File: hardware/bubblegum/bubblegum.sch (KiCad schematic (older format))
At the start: 107 parts, among them P1 RX_OUT, P2 RX_ONLY, P3 SERIAL, P4 TX/RX, P5 CONN_2, P6 TX_IN, P7 VCC, P8 SWITCH_CTRL, Q1 MOSFET_P, Q2 MOSFET_N, Q3 MOSFET_P, Q4 MOSFET_N, T1 RX_IF_BALUN, T2 RX_BALUN, T4 TX_BALUN, T6 TX_IF_BALUN, U10 TX_HIGHPASS_FILTER, U11 PE4140, U12 SKY13350, U13 TX_LOWPASS_FILTER, U16 GSG-74HC04, U3 RX_HIGHPASS_FILTER, U4 SKY13350, U5 SKY13350, U6 PE4140, U7 RX_LOWPASS_FILTER, U8 SKY13350, U9 TRF3765

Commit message: loop filter values for PFD at 1.6 MHz
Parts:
- C31: value C -> 47pF
- C32: value C -> 560pF
- C33: value C -> 4p7
- C34: value C -> DNP
- R13: value R -> 10k
- R6: value R -> 5k
- R7: value R -> 0
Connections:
- wire segments 354 -> 355
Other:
- note added: "loop filter\n(1.6 MHz)"
- note removed: "loop filter"

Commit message: noticed bias problem with LO bypass mode
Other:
- note added: "FIXME: This should be pulled below GND in bypass\nmode, or perhaps everything could be biased to 1V8\nin normal mode."
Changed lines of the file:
@@
-EESchema Schematic File Version 2  date Sat Jun 30 12:21:44 2012
+EESchema Schematic File Version 2  date Sun Jul  1 07:30:52 2012
 LIBS:power
 LIBS:device
@@
 Sheet 1 1
 Title ""
-Date "30 jun 2012"
+Date "1 jul 2012"
 Rev ""
 Comp ""
@@
 Comment4 ""
 $EndDescr
+Text Notes 11100 2450 0    40   ~ 0
+FIXME: This should be pulled below GND in bypass\nmode, or perhaps everything could be biased to 1V8\nin normal mode.
 Connection ~ 13600 6050
 Wire Wire Line

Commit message: fixed LO bypass mode by introducing intermediate mixer bias voltage
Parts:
- removed Q1, Q3: MOSFET_P, symbol MOSFET_P
- removed Q2, Q4, Q? (x2): MOSFET_N, symbol MOSFET_N
- removed R1, R8: 10k, symbol R
- added C? (x2): 1uF, symbol C
- added C? (x8): 100nF, symbol C
- added U? (x2): DMC2400, symbol DMC2400
- added U? (x2): DMN2400, symbol DMC2400
- added U?: NCP699, symbol NCP699
- L3, L4, L5, L6: value INDUCTOR -> 4n7
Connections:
- net labels added: MIX_BIAS, RX_BYPASS, TX_BYPASS
- wire segments 355 -> 406
- no-connect marks 11 -> 9
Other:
- note added: "Bypass control signals allow the LO to be\nbypassed (essentially a zero Hz LO). The LO\nshould be switched off when bypass is enabled."
- note added: "DC connection to MIX_BIAS\nrequired on IF1, IF2?"
- note added: "DC connection to MIX_BIAS\nrequired on RF1, RF2?"
- note added: "balun here may not be needed if\ndirect connection to MAX2837 is made"
- note removed: "Bypass control signals (active low) allow the LO to\nbe bypassed (essentially a zero Hz LO). The LO\nshould be switched off when bypass is enabled."
- note removed: "DC connection to GND required on IF1, IF2?"
- note removed: "DC connection to GND required on RF1, RF2?"
- note removed: "FIXME: This should be pulled below GND in bypass\nmode, or perhaps everything could be biased to 1V8\nin normal mode."
- note removed: "balun here may not not be needed if\ndirect connection to MAX2837 is made"
- moved on the sheet: C?, L6

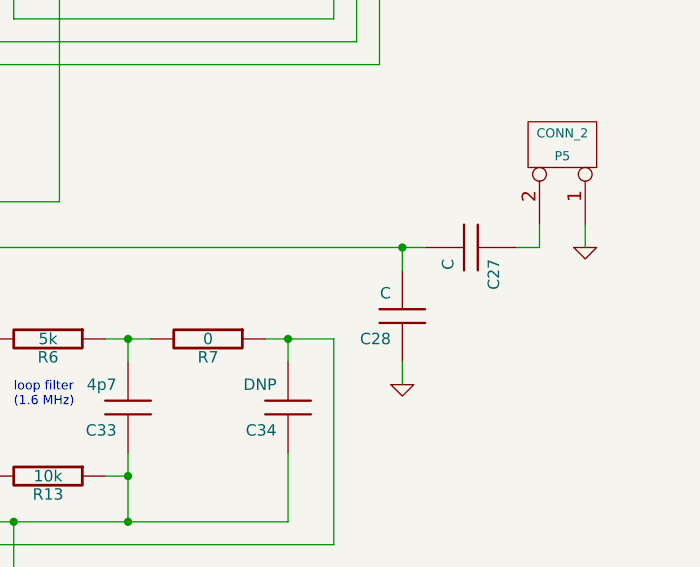
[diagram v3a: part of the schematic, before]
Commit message: reference clock divider
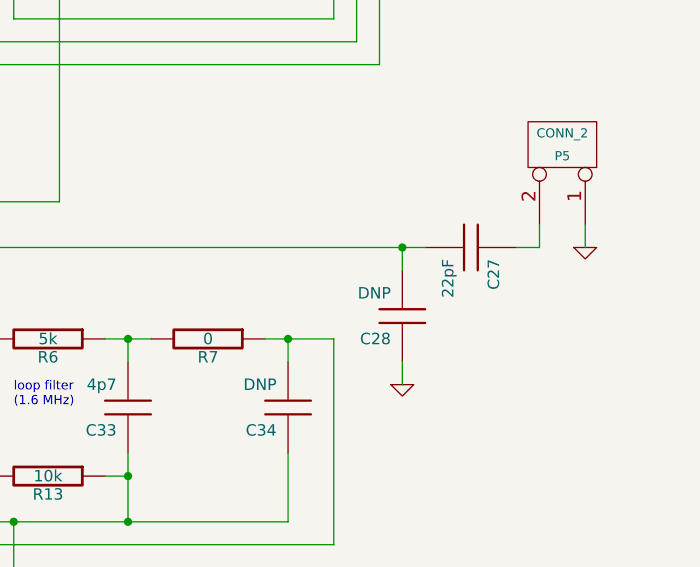
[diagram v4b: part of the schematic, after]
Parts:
- C27: value C -> 22pF
- C28: value C -> DNP
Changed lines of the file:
@@
-EESchema Schematic File Version 2  date Sun Jul  1 13:58:34 2012
+EESchema Schematic File Version 2  date Sun Jul  1 14:26:11 2012
 LIBS:power
 LIBS:device
@@
 P 15300 5150
 F 0 "C28" H 15350 5250 50  0000 L CNN
-F 1 "C" H 15350 5050 50  0000 L CNN
+F 1 "DNP" H 15350 5050 50  0000 L CNN
 	1    15300 5150
 	-1   0    0    1
@@
 P 15600 4850
 F 0 "C27" H 15650 4950 50  0000 L CNN
-F 1 "C" H 15650 4750 50  0000 L CNN
+F 1 "22pF" H 15650 4750 50  0000 L CNN
 	1    15600 4850
 	0    1    1    0

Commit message: renamed switch signals - hopefully clearer
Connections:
- net SWD1 renamed TX_ANT
- net SWD2 renamed !TX_ANT
- net SWRX1 renamed RX_LP
- net RX_LP: now also U16.4 (2Y); no longer P8.5, U16.3 (2A)
- net SWRX2 renamed RX_HP
- net RX_HP: now also P8.5, U16.3 (2A); no longer U16.4 (2Y)
- net SWTX1 renamed TX_LP
- net TX_LP: now also U16.2 (1Y); no longer P8.7, U16.1 (1A)
- net SWTX2 renamed TX_HP
- net TX_HP: now also P8.7, U16.1 (1A); no longer U16.2 (1Y)

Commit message: updated Anaren balun topology
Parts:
- removed T2: RX_BALUN, symbol BALUN
- removed T4: TX_BALUN, symbol BALUN
- added T2: RX_BALUN, symbol BALUN-B0310J50100AHF
- added T4: TX_BALUN, symbol BALUN-B0310J50100AHF
- C10, C61: renamed from C?; value 100nF -> 10nF
- gave numbers to parts that had none: 26
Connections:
- net MIX_BIAS: no longer C10.1, C61.1
- net at C60.2: now also T4.1 (S1)
- net at U11.1 (IF1): now also T4.3 (PR1)
- net at U11.6 (IF2): now also T4.4 (PR2)
- net at U6.2 (RF1): now also T2.4 (PR2)
- net at U6.3 (RF2): now also T2.3 (PR1)
- net at C7.2: now also T2.1 (S1)
- new net: C61.1, T4.2 (S2)
- new net: C10.1, T2.2 (S2)
- no-connect marks 9 -> 7
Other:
- moved on the sheet: C10, C13, C61, C7

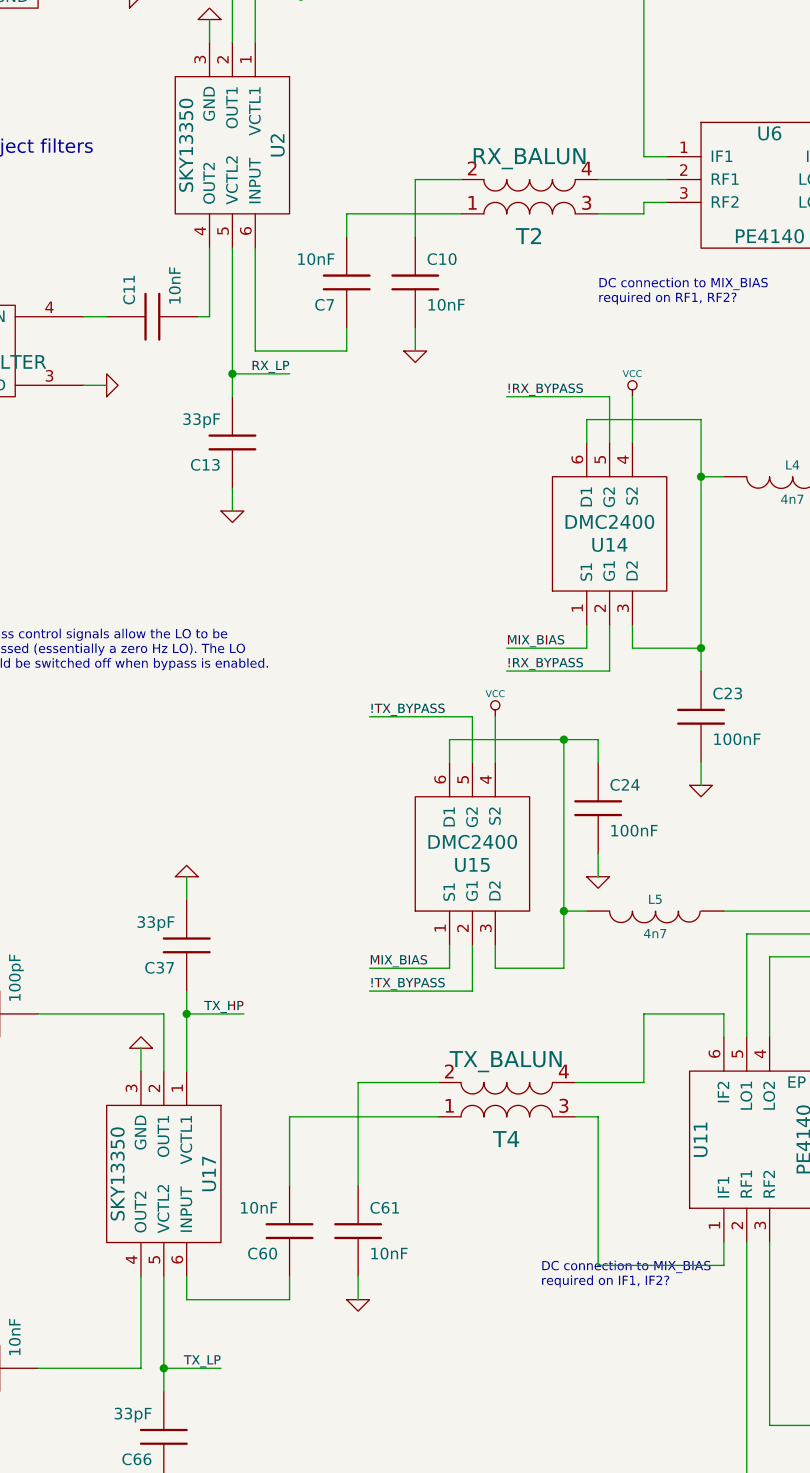
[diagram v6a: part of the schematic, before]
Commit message: fixed balun bias
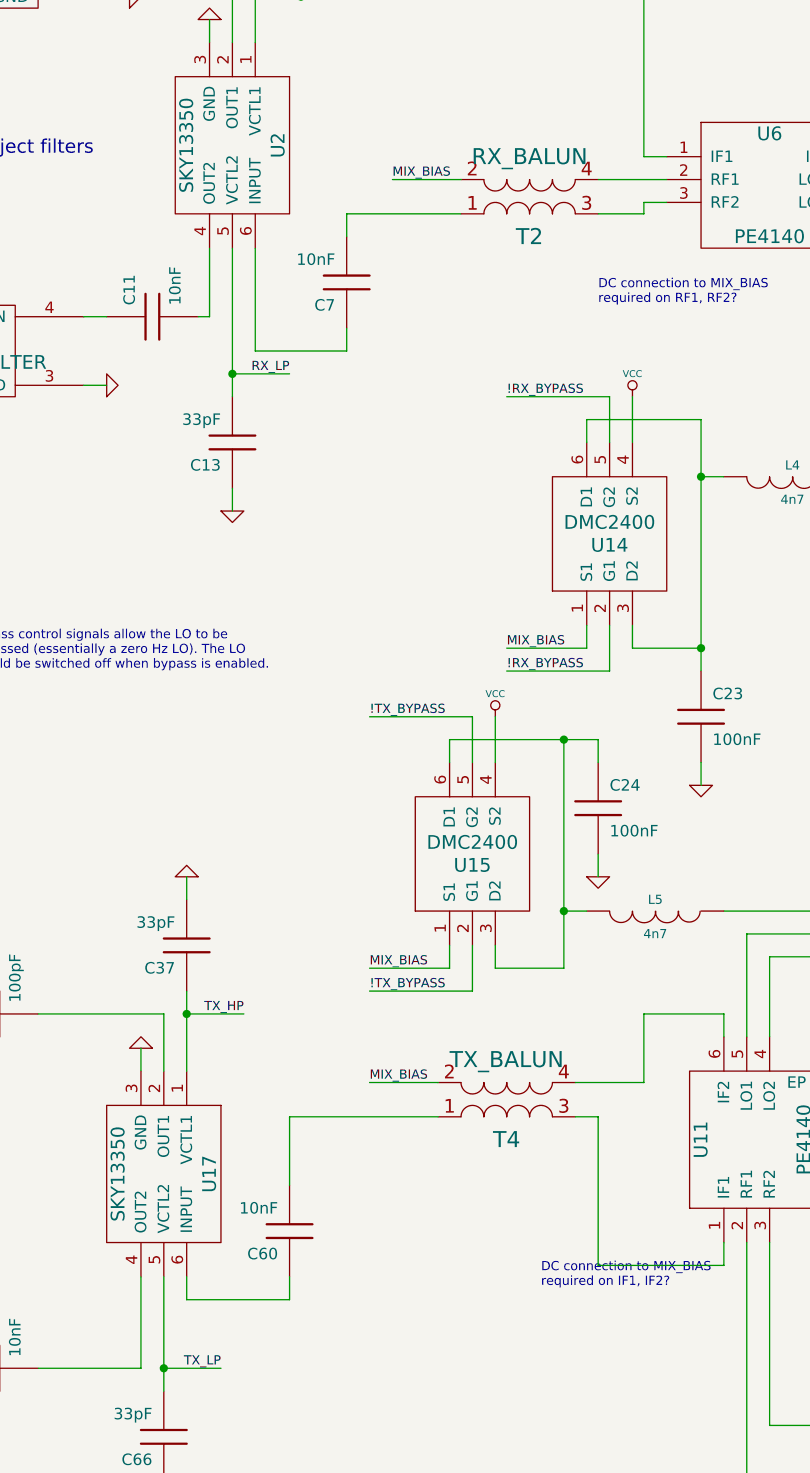
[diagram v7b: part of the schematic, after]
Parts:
- removed C10, C61: 10nF, symbol C
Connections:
- net MIX_BIAS: now also T2.2 (S2), T4.2 (S2)
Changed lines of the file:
@@
-EESchema Schematic File Version 2  date Thu Jul  5 17:46:43 2012
+EESchema Schematic File Version 2  date Thu Jul  5 17:58:03 2012
 LIBS:power
 LIBS:device
@@
 Comment4 ""
 $EndDescr
-Wire Wire Line
-	7400 2850 7400 3100
-Wire Wire Line
-	7600 2850 7400 2850
+Text Label 7200 6800 0    40   ~ 0
+MIX_BIAS
+Text Label 7300 2850 0    40   ~ 0
+MIX_BIAS
+Wire Wire Line
+	7600 2850 7300 2850
 Wire Wire Line
 	8200 3000 8400 3000
@@
 	11800 2450 11800 2350
 Wire Wire Line
-	7400 3600 7400 3500
-Wire Wire Line
 	11750 9300 11750 9200
-Wire Wire Line
-	7150 7750 7150 7650
 Wire Wire Line
 	8250 10200 8250 10100
@@
 Wire Wire Line
 	2700 9900 3100 9900
-Wire Wire Line
-	7150 7250 7150 6800
 Connection ~ 10600 2250
 Wire Wire Line
@@
 	8750 7600 8750 7500
 Wire Wire Line
-	7150 6800 7500 6800
+	7200 6800 7500 6800
 Wire Wire Line
 	6050 3750 5950 3750
@@
 $EndComp
 $Comp
-L GND #PWR16
-U 1 1 4FF0A50C
-P 7400 3600
-F 0 "#PWR16" H 7400 3600 30  0001 C CNN
-F 1 "GND" H 7400 3530 30  0001 C CNN
-	1    7400 3600
-	1    0    0    -1
-$EndComp
-$Comp
-L C C10
-U 1 1 4FF0A4DC
-P 7400 3300
-F 0 "C10" H 7450 3400 50  0000 L CNN
-F 1 "10nF" H 7450 3200 50  0000 L CNN
-	1    7400 3300
-	1    0    0    -1
-$EndComp
-$Comp
 L GND #PWR72
 U 1 1 4FF0A4BF
@@
 	1    0    0    -1
 $EndComp
-$Comp
-L GND #PWR60
-U 1 1 4FF0A4AE
-P 7150 7750
-F 0 "#PWR60" H 7150 7750 30  0001 C CNN
-F 1 "GND" H 7150 7680 30  0001 C CNN
-	1    7150 7750
-	1    0    0    -1
-$EndComp
-$Comp
-L C C61
-U 1 1 4FF0A494
-P 7150 7450
-F 0 "C61" H 7200 7550 50  0000 L CNN
-F 1 "10nF" H 7200 7350 50  0000 L CNN
-	1    7150 7450
-	1    0    0    -1
-$EndComp

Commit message: reworked balun bias again
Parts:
- added C10, C61: 10nF, symbol C
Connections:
- net GND: now also C10.2, C61.2
- net MIX_BIAS: now also C10.1, C61.1
